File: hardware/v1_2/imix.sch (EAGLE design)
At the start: 151 parts, among them J2_3_5_AND_6 ARDUINO_R3NO_HOLES, Q2 AO3415, Q3 AO3415, Q4 AO3415, Q5 AO3415, U1 BQ2423X, U10 ISL29035, U11 FX0S8700CQ, U12 296-12686-1-ND, U3 TLV3202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

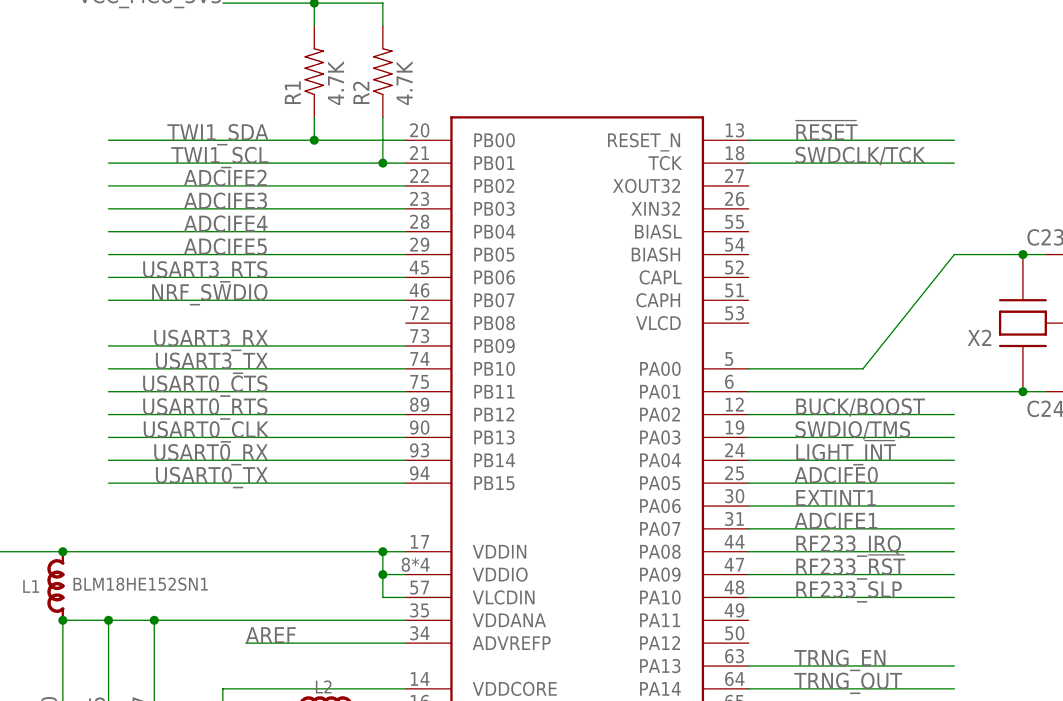
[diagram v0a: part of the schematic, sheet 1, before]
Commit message: Correct ADC numbering in doc. Closes #16
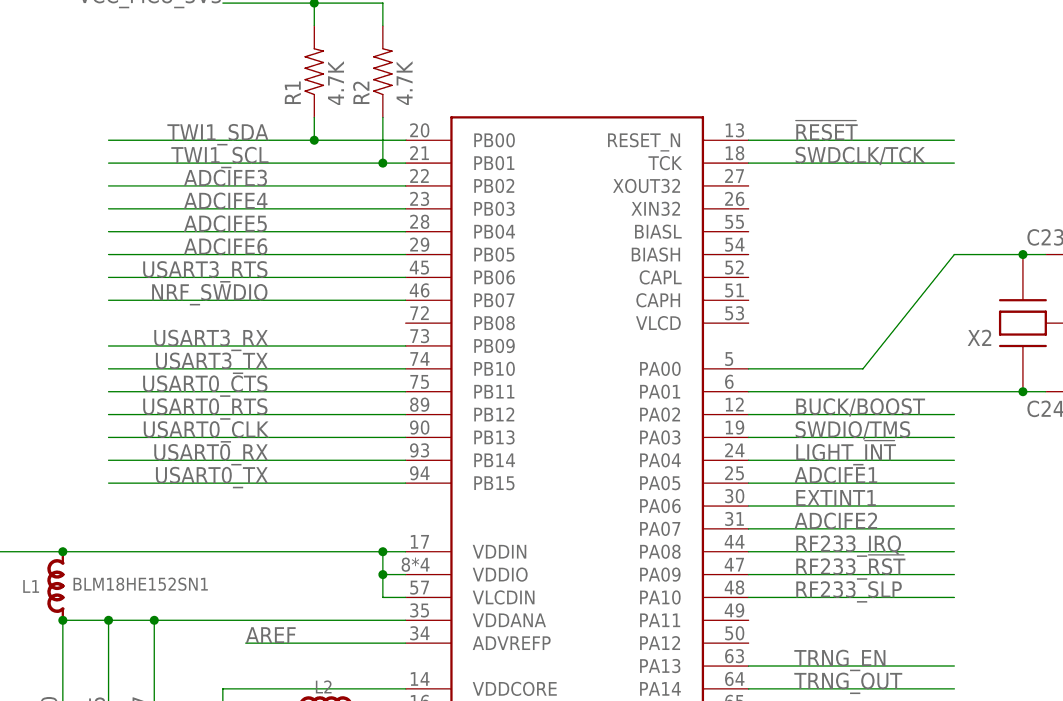
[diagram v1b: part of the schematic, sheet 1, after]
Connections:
- removed net ADCIFE0: J2_3_5_AND_6.A0, U6.PA05
- new net ADCIFE6: J2_3_5_AND_6.A5, U6.PB05
- net ADCIFE1: now also J2_3_5_AND_6.A0, U6.PA05; no longer J2_3_5_AND_6.A1, U6.PA07
- net ADCIFE2: now also J2_3_5_AND_6.A1, U6.PA07; no longer J2_3_5_AND_6.A2, U6.PB02
- net ADCIFE3: now also J2_3_5_AND_6.A2, U6.PB02; no longer J2_3_5_AND_6.A3, U6.PB03
- net ADCIFE4: now also J2_3_5_AND_6.A3, U6.PB03; no longer J2_3_5_AND_6.A4, U6.PB04
- net ADCIFE5: now also J2_3_5_AND_6.A4, U6.PB04; no longer J2_3_5_AND_6.A5, U6.PB05
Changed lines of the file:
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@@
 </segment>
 </net>
-<net name="ADCIFE0" class="0">
+<net name="ADCIFE1" class="0">
 <segment>
 <wire x1="121.92" y1="134.62" x2="144.78" y2="134.62" width="0.1524" layer="91"/>
@@
 </segment>
 </net>
-<net name="ADCIFE1" class="0">
+<net name="ADCIFE2" class="0">
 <segment>
 <wire x1="121.92" y1="129.54" x2="144.78" y2="129.54" width="0.1524" layer="91"/>
@@
 </segment>
 </net>
-<net name="ADCIFE2" class="0">
+<net name="ADCIFE3" class="0">
 <segment>
 <wire x1="83.82" y1="167.64" x2="50.8" y2="167.64" width="0.1524" layer="91"/>
@@
 </segment>
 </net>
-<net name="ADCIFE3" class="0">
+<net name="ADCIFE4" class="0">
 <segment>
 <wire x1="83.82" y1="165.1" x2="50.8" y2="165.1" width="0.1524" layer="91"/>
@@
 </segment>
 </net>
-<net name="ADCIFE4" class="0">
+<net name="ADCIFE5" class="0">
 <segment>
 <wire x1="83.82" y1="162.56" x2="50.8" y2="162.56" width="0.1524" layer="91"/>
@@
 </segment>
 </net>
-<net name="ADCIFE5" class="0">
+<net name="ADCIFE6" class="0">
 <segment>
 <wire x1="83.82" y1="160.02" x2="50.8" y2="160.02" width="0.1524" layer="91"/>
@@
 </segment>
 </net>
-<net name="ADCIFE5" class="0">
+<net name="ADCIFE6" class="0">
 <segment>
 <wire x1="182.88" y1="127" x2="170.18" y2="127" width="0.1524" layer="91"/>
@@
 </segment>
 </net>
-<net name="ADCIFE0" class="0">
+<net name="ADCIFE1" class="0">
 <segment>
 <wire x1="182.88" y1="139.7" x2="170.18" y2="139.7" width="0.1524" layer="91"/>
@@
 </segment>
 </net>
-<net name="ADCIFE1" class="0">
+<net name="ADCIFE2" class="0">
 <segment>
 <wire x1="182.88" y1="137.16" x2="170.18" y2="137.16" width="0.1524" layer="91"/>
@@
 </segment>
 </net>
-<net name="ADCIFE2" class="0">
+<net name="ADCIFE3" class="0">
 <segment>
 <wire x1="182.88" y1="134.62" x2="170.18" y2="134.62" width="0.1524" layer="91"/>
@@
 </segment>
 </net>
-<net name="ADCIFE3" class="0">
+<net name="ADCIFE4" class="0">
 <segment>
 <wire x1="182.88" y1="132.08" x2="170.18" y2="132.08" width="0.1524" layer="91"/>
@@
 </segment>
 </net>
-<net name="ADCIFE4" class="0">
+<net name="ADCIFE5" class="0">
 <segment>
 <wire x1="182.88" y1="129.54" x2="170.18" y2="129.54" width="0.1524" layer="91"/>
